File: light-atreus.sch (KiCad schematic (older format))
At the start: 11 parts, among them J2 CONN_01X02, J3 CONN_01X02, J5 CONN_01X02, J6 CONN_01X02

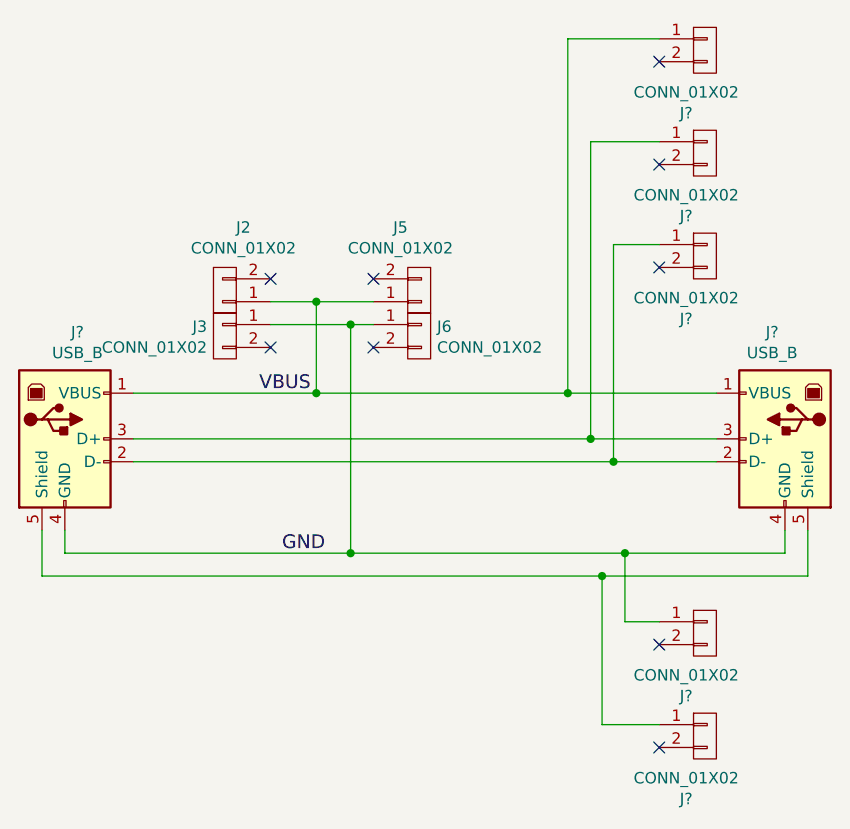
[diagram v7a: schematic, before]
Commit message: Regen netlist with correct part footprints
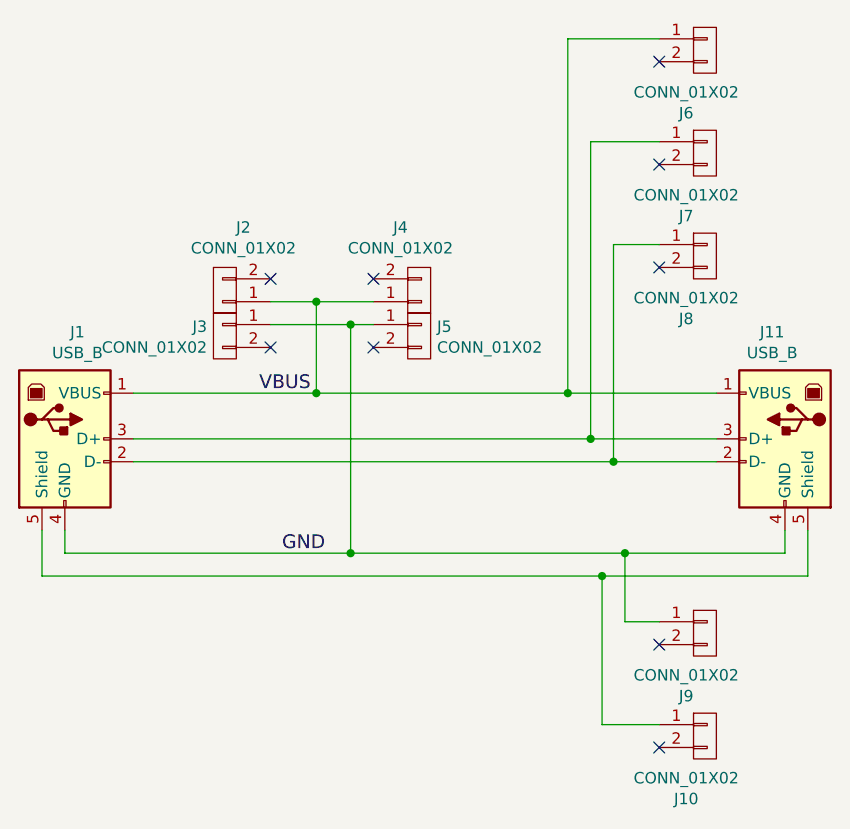
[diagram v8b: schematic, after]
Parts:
- J11: renamed from J?; footprint (none) -> custom_footprints:USB_Micro-B-custom-plug
- gave numbers to parts that had none: 6
- renumbered J5 to J4, J6 to J5
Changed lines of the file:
@@
 $EndComp
 $Comp
-L CONN_01X02 J5
+L CONN_01X02 J4
 U 1 1 59CAC690
 P 5050 3200
-F 0 "J5" H 4968 2925 50  0000 C CNN
+F 0 "J4" H 4968 2925 50  0000 C CNN
 F 1 "CONN_01X02" H 4968 3016 50  0000 C CNN
 F 2 "custom_footprints:SolderWirePad_1x2-8mm" H 5050 3200 50  0001 C CNN
@@
 $EndComp
 $Comp
-L CONN_01X02 J6
+L CONN_01X02 J5
 U 1 1 59CAC6F5
 P 5050 3400
-F 0 "J6" H 5128 3441 50  0000 L CNN
+F 0 "J5" H 5128 3441 50  0000 L CNN
 F 1 "CONN_01X02" H 5128 3350 50  0000 L CNN
 F 2 "custom_footprints:SolderWirePad_1x2-8mm" H 5050 3400 50  0001 C CNN
@@
 VBUS
 $Comp
-L USB_B J?
+L USB_B J1
 U 1 1 59CD5E46
 P 3500 3850
-F 0 "J?" H 3555 4317 50  0000 C CNN
+F 0 "J1" H 3555 4317 50  0000 C CNN
 F 1 "USB_B" H 3555 4226 50  0000 C CNN
 F 2 "custom_footprints:USB_Micro-B-custom" H 3650 3800 50  0001 C CNN
@@
 $EndComp
 $Comp
-L USB_B J?
+L USB_B J11
 U 1 1 59CD612E
 P 6650 3850
-F 0 "J?" H 6706 4317 50  0000 C CNN
+F 0 "J11" H 6706 4317 50  0000 C CNN
 F 1 "USB_B" H 6706 4226 50  0000 C CNN
-F 2 "" H 6800 3800 50  0001 C CNN
+F 2 "custom_footprints:USB_Micro-B-custom-plug" H 6800 3800 50  0001 C CNN
 F 3 "" H 6800 3800 50  0001 C CNN
 	1    6650 3850
@@
 $EndComp
 $Comp
-L CONN_01X02 J?
+L CONN_01X02 J8
 U 1 1 59CD62AF
 P 6300 3050
-F 0 "J?" H 6218 2775 50  0000 C CNN
+F 0 "J8" H 6218 2775 50  0000 C CNN
 F 1 "CONN_01X02" H 6218 2866 50  0000 C CNN
 F 2 "custom_footprints:SolderWirePad_1x2-8mm" H 6300 3050 50  0001 C CNN
@@
 	6750 4450 6750 4250
 $Comp
-L CONN_01X02 J?
+L CONN_01X02 J7
 U 1 1 59CD64BA
 P 6300 2600
-F 0 "J?" H 6218 2325 50  0000 C CNN
+F 0 "J7" H 6218 2325 50  0000 C CNN
 F 1 "CONN_01X02" H 6218 2416 50  0000 C CNN
 F 2 "custom_footprints:SolderWirePad_1x2-8mm" H 6300 2600 50  0001 C CNN
@@
 $EndComp
 $Comp
-L CONN_01X02 J?
+L CONN_01X02 J9
 U 1 1 59CD6590
 P 6300 4700
-F 0 "J?" H 6218 4425 50  0000 C CNN
+F 0 "J9" H 6218 4425 50  0000 C CNN
 F 1 "CONN_01X02" H 6218 4516 50  0000 C CNN
 F 2 "custom_footprints:SolderWirePad_1x2-8mm" H 6300 4700 50  0001 C CNN
@@
 $EndComp
 $Comp
-L CONN_01X02 J?
+L CONN_01X02 J10
 U 1 1 59CD667D
 P 6300 5150
-F 0 "J?" H 6218 4875 50  0000 C CNN
+F 0 "J10" H 6218 4875 50  0000 C CNN
 F 1 "CONN_01X02" H 6218 4966 50  0000 C CNN
 F 2 "custom_footprints:SolderWirePad_1x2-8mm" H 6300 5150 50  0001 C CNN
@@
 $EndComp
 $Comp
-L CONN_01X02 J?
+L CONN_01X02 J6
 U 1 1 59CD691B
 P 6300 2150
-F 0 "J?" H 6218 1875 50  0000 C CNN
+F 0 "J6" H 6218 1875 50  0000 C CNN
 F 1 "CONN_01X02" H 6218 1966 50  0000 C CNN
 F 2 "custom_footprints:SolderWirePad_1x2-8mm" H 6300 2150 50  0001 C CNN
